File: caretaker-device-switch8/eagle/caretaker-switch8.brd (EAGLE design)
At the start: 160 x 100 mm, 61 parts, among them IC2 ATmega168-20PU, IC4 MCP1702-5002, IC5 MCP1702-3302, K1 S202S02, K2 S202S02, K3 S202S02, K4 S202S02, K5 S202S02, K6 S202S02, K7 S202S02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

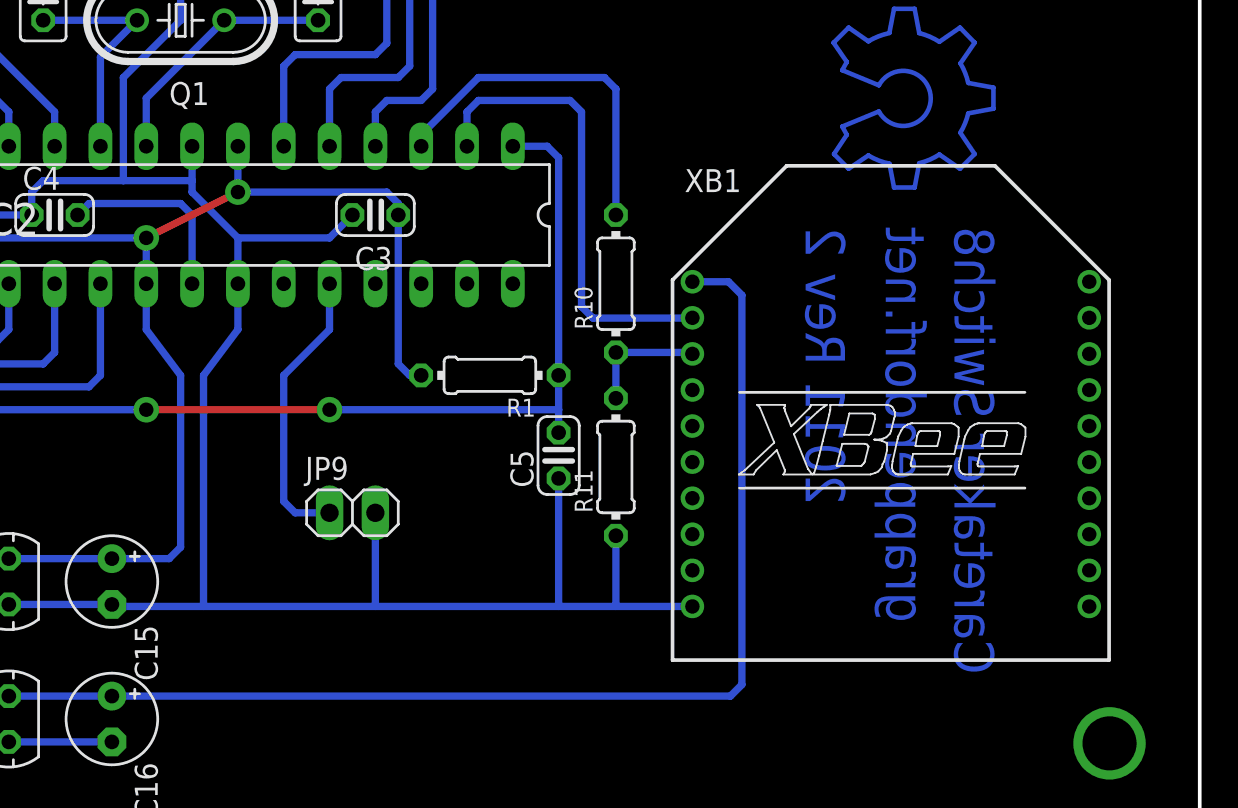
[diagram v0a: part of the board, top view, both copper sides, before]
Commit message: feat: Convert the XBee Switch8 device to a WLAN device
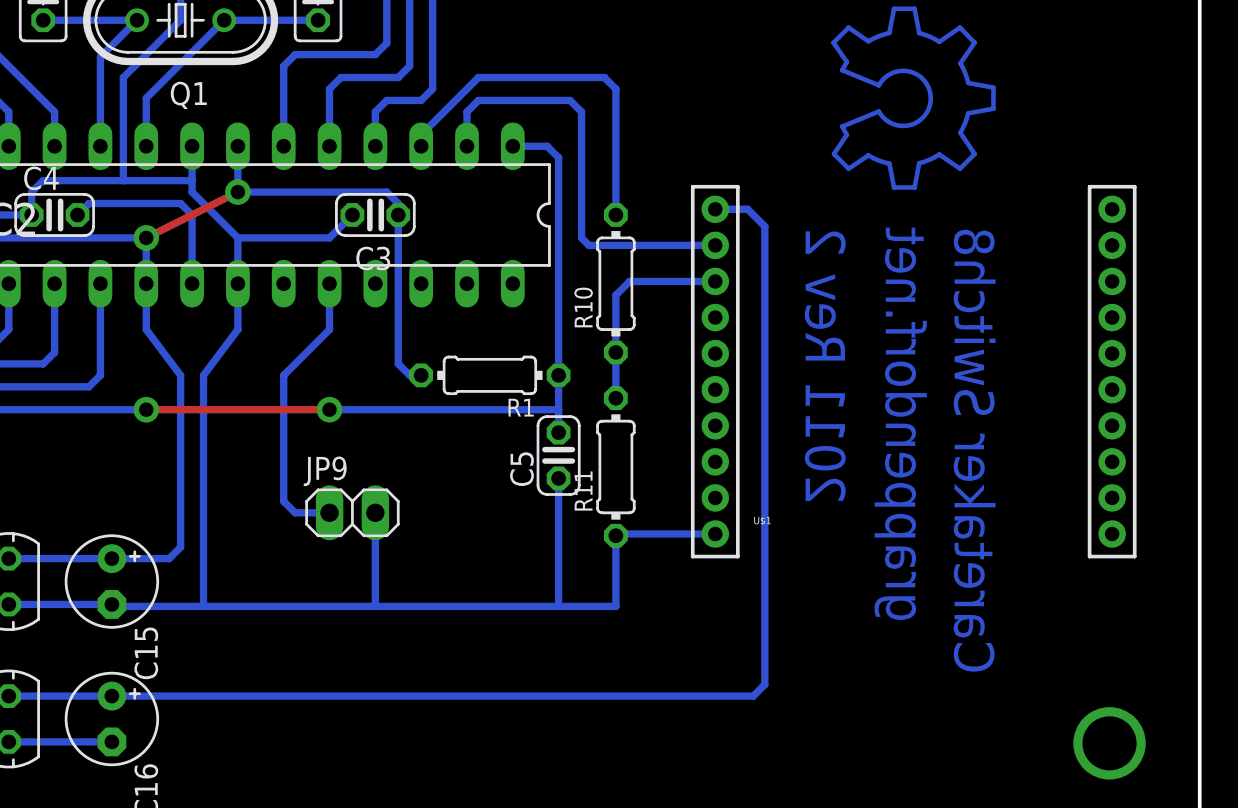
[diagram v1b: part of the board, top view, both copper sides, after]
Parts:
- removed XB1: XBEE, maxstream:XBEE
- added U$1: WIFLY-TH, grapelabs:WIFLY-TH
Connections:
- net +3V3: now also U$1.1; no longer XB1.1
- net GND: now also U$1.10; no longer XB1.10
- net N$49: now also U$1.3; no longer XB1.3
- net RXD: now also U$1.2; no longer XB1.2
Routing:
- net +3V3: track 65.5 -> 70.7 mm
- net N$49: track 6.97 -> 11.5 mm
- net RXD: track 26.0 -> 23.4 mm
- net GND: track 389.1 -> 390.5 mm
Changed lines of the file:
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@@
 <layer number="54" name="bGND_GNDA" color="1" fill="9" visible="no" active="no"/>
 <layer number="56" name="wert" color="7" fill="1" visible="no" active="yes"/>
+<layer number="60" name="Board" color="7" fill="1" visible="yes" active="yes"/>
 <layer number="91" name="Nets" color="2" fill="1" visible="no" active="no"/>
 <layer number="92" name="Busses" color="1" fill="1" visible="no" active="no"/>
@@
 </element>
 <element name="X1" library="con-wago-500" package="W237-103" value="" x="7.62" y="57.15" rot="R90"/>
-<element name="XB1" library="maxstream" package="XBEE" value="XBEE" x="142.875" y="21.59" smashed="yes">
-<attribute name="NAME" x="131.445" y="35.56" size="1.27" layer="25"/>
-<attribute name="VALUE" x="131.445" y="7.62" size="1.27" layer="27"/>
-</element>
 <element name="B1" library="rectifier" package="2KBB" value="B40C1500" x="64.135" y="12.7" rot="R270"/>
 <element name="K1" library="relay" package="S202S02" value="S202S02" x="24.13" y="73.66" rot="R270"/>
@@
 <element name="R11" library="rcl" package="0204/7" value="15k" x="127.635" y="20.32" rot="R90"/>
 <element name="JP9" library="pinhead" package="1X02" value="BUZZER" x="113.03" y="17.78"/>
+<element name="U$1" library="grapelabs" package="WIFLY-TH" value="WIFLY-TH" x="144.145" y="14.605"/>
 </elements>
 <signals>
@@
 <contactref element="C5" pad="1"/>
 <contactref element="C4" pad="1"/>
-<contactref element="XB1" pad="10"/>
 <contactref element="ISP" pad="6"/>
 <contactref element="K1" pad="4"/>
@@
 <wire x1="114.3" y1="12.59" x2="124.46" y2="12.59" width="0.4064" layer="16"/>
 <wire x1="124.46" y1="12.59" x2="127.635" y2="12.59" width="0.4064" layer="16"/>
-<wire x1="127.635" y1="12.59" x2="131.875" y2="12.59" width="0.4064" layer="16"/>
 <wire x1="99.695" y1="12.7" x2="99.805" y2="12.59" width="0.4064" layer="16"/>
 <wire x1="127.635" y1="12.59" x2="127.635" y2="16.51" width="0.4064" layer="16"/>
@@
 <via x="81.915" y="34.29" extent="1-16" drill="0.8" diameter="1.4224"/>
 <via x="88.9" y="34.29" extent="1-16" drill="0.8" diameter="1.4224"/>
+<contactref element="U$1" pad="10"/>
+<contactref element="U$1" pad="10"/>
+<wire x1="133.145" y1="16.605" x2="127.73" y2="16.605" width="0.4064" layer="16"/>
+<wire x1="127.73" y1="16.605" x2="127.635" y2="16.51" width="0.4064" layer="16"/>
 </signal>
 <signal name="N$1">
@@
 </signal>
 <signal name="+3V3">
-<contactref element="XB1" pad="1"/>
 <contactref element="C16" pad="+"/>
 <contactref element="IC5" pad="VOUT"/>
 <wire x1="93.98" y1="7.62" x2="99.695" y2="7.62" width="0.4064" layer="16"/>
-<wire x1="99.695" y1="7.62" x2="133.985" y2="7.62" width="0.4064" layer="16"/>
-<wire x1="133.985" y1="7.62" x2="134.62" y2="8.255" width="0.4064" layer="16"/>
-<wire x1="133.875" y1="30.59" x2="131.875" y2="30.59" width="0.4064" layer="16"/>
-<wire x1="134.62" y1="29.845" x2="133.875" y2="30.59" width="0.4064" layer="16"/>
-<wire x1="134.62" y1="8.255" x2="134.62" y2="29.845" width="0.4064" layer="16"/>
+<contactref element="U$1" pad="1"/>
+<wire x1="99.695" y1="7.62" x2="135.255" y2="7.62" width="0.4064" layer="16"/>
+<wire x1="135.255" y1="7.62" x2="135.89" y2="8.255" width="0.4064" layer="16"/>
+<wire x1="133.145" y1="34.605" x2="134.94" y2="34.605" width="0.4064" layer="16"/>
+<wire x1="134.94" y1="34.605" x2="135.89" y2="33.655" width="0.4064" layer="16"/>
+<wire x1="135.89" y1="33.655" x2="135.89" y2="8.255" width="0.4064" layer="16"/>
 </signal>
 <signal name="RESET">
@@
 </signal>
 <signal name="RXD">
-<contactref element="XB1" pad="2"/>
 <contactref element="IC2" pad="2"/>
 <wire x1="119.38" y1="40.005" x2="119.38" y2="38.1" width="0.4064" layer="16"/>
@@
 <wire x1="125.095" y1="40.64" x2="120.015" y2="40.64" width="0.4064" layer="16"/>
 <wire x1="125.73" y1="40.005" x2="125.095" y2="40.64" width="0.4064" layer="16"/>
-<wire x1="125.73" y1="29.21" x2="125.73" y2="40.005" width="0.4064" layer="16"/>
-<wire x1="126.365" y1="28.575" x2="125.73" y2="29.21" width="0.4064" layer="16"/>
-<wire x1="126.365" y1="28.575" x2="131.86" y2="28.575" width="0.4064" layer="16"/>
-<wire x1="131.86" y1="28.575" x2="131.875" y2="28.59" width="0.4064" layer="16"/>
+<contactref element="U$1" pad="2"/>
+<wire x1="133.145" y1="32.605" x2="126.145" y2="32.605" width="0.4064" layer="16"/>
+<wire x1="126.145" y1="32.605" x2="125.73" y2="33.02" width="0.4064" layer="16"/>
+<wire x1="125.73" y1="33.02" x2="125.73" y2="40.005" width="0.4064" layer="16"/>
 </signal>
 <signal name="TXD">
@@
 <contactref element="R10" pad="1"/>
 <contactref element="R11" pad="2"/>
-<contactref element="XB1" pad="3"/>
-<wire x1="127.635" y1="26.67" x2="131.955" y2="26.67" width="0.4064" layer="16"/>
-<wire x1="131.955" y1="26.67" x2="131.875" y2="26.59" width="0.4064" layer="16"/>
 <wire x1="127.635" y1="24.13" x2="127.635" y2="26.67" width="0.4064" layer="16"/>
+<contactref element="U$1" pad="3"/>
+<wire x1="133.145" y1="30.605" x2="128.395" y2="30.605" width="0.4064" layer="16"/>
+<wire x1="128.395" y1="30.605" x2="127.635" y2="29.845" width="0.4064" layer="16"/>
+<wire x1="127.635" y1="29.845" x2="127.635" y2="26.67" width="0.4064" layer="16"/>
 </signal>
 <signal name="N$42">
